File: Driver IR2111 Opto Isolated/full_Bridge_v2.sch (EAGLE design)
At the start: 20 parts

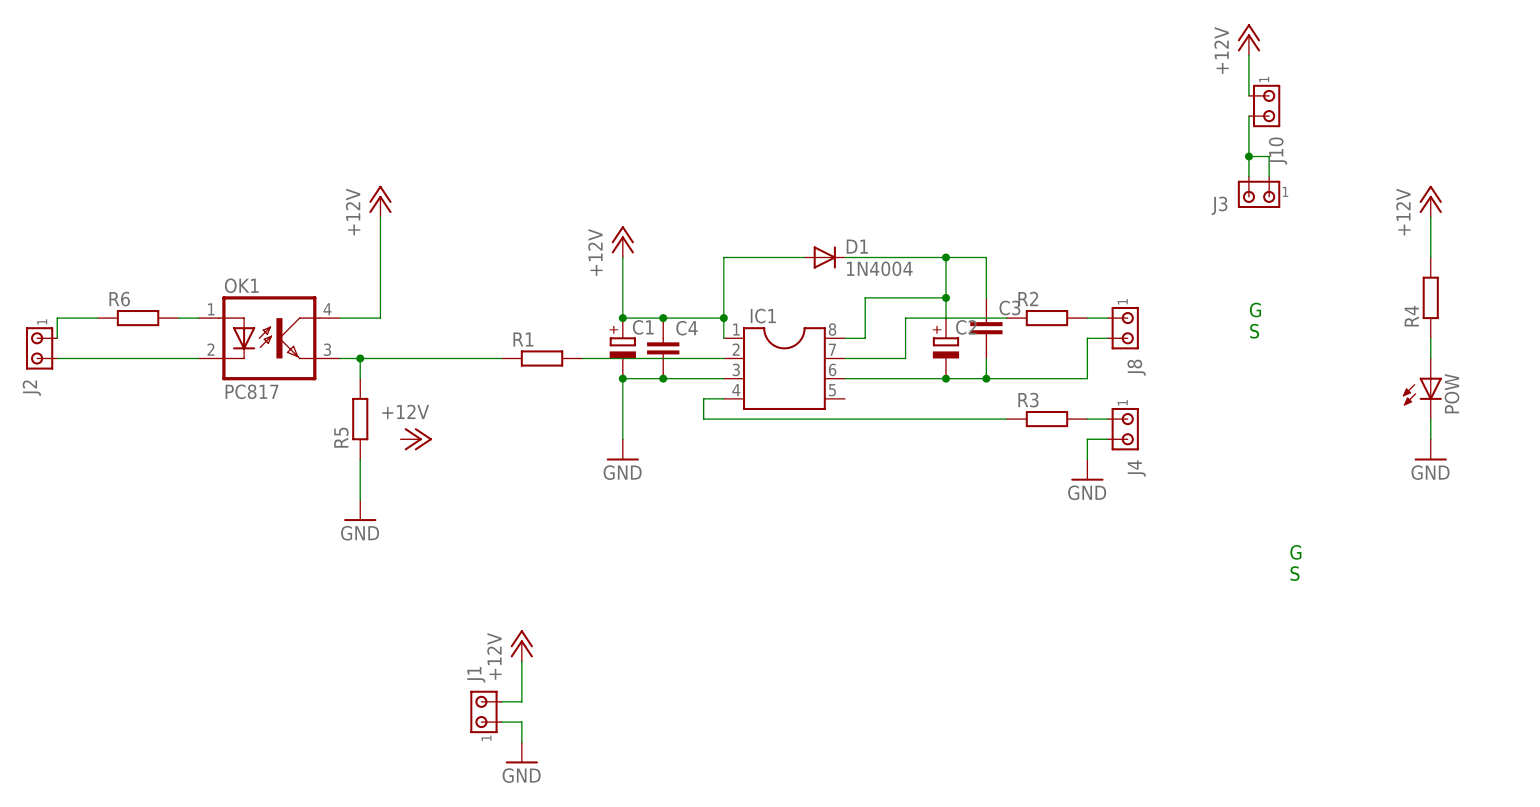
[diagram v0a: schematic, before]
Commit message: IR2111 optical isolated driver updated
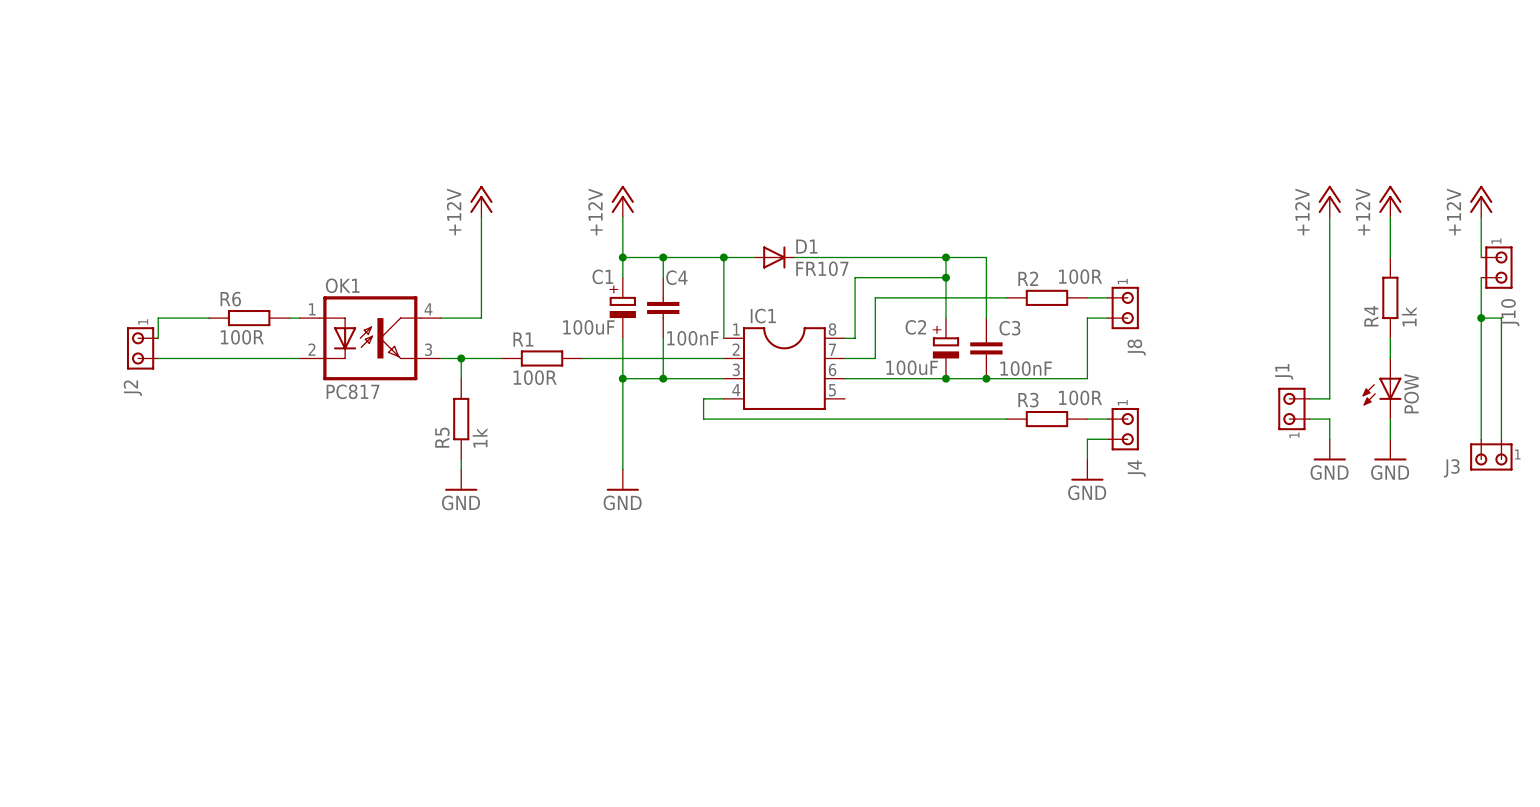
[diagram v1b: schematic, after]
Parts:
- C1, C2: value (none) -> 100uF
- C3, C4: value (none) -> 100nF
- D1: value 1N4004 -> FR107
- R1, R2, R3, R6: value (none) -> 100R
- R4, R5: value (none) -> 1k
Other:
- note removed: "G S"
- moved on the sheet: C1, C3, C4, D1, J1, J10, J2, J3, J8, OK1, POW, R2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
